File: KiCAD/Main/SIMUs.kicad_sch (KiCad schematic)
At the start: 10 parts, among them U14 BMI270, U15 BMI270, U16 BMI270

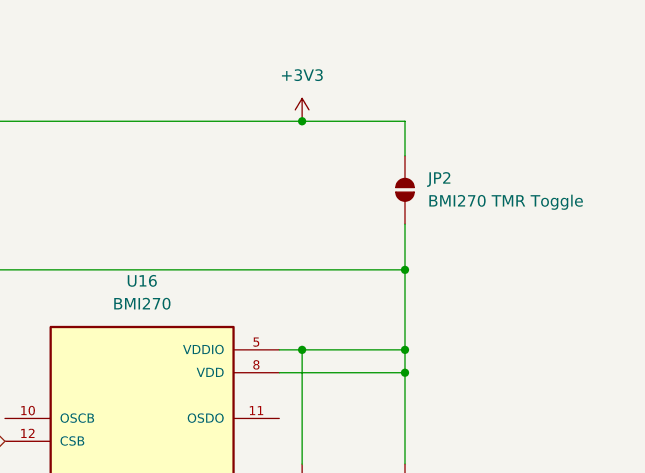
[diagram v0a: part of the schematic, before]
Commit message: Moved custom footprints into local KiCAD footprint library
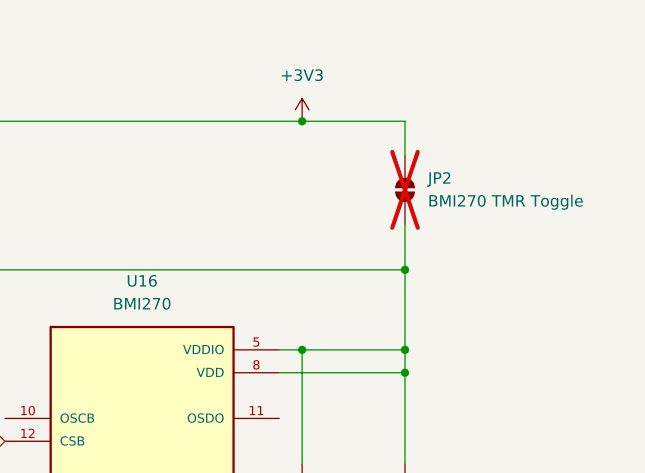
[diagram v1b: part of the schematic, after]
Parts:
- JP2: footprint Resistor_SMD:R_0603_1608Metric_Pad0.98x0.95mm_HandSolder -> Jumper:SolderJumper-2_P1.3mm_Open_TrianglePad1.0x1.5mm; now not fitted
- U14, U15, U16: footprint BMI270:XDCR_BMI270 -> LRI:XDCR_BMI270
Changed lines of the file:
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@@
 			)
 		)
-		(property "Footprint" "BMI270:XDCR_BMI270"
+		(property "Footprint" "LRI:XDCR_BMI270"
 			(at 157.48 106.68 0)
 			(effects
@@
 			)
 		)
-		(property "Footprint" "BMI270:XDCR_BMI270"
+		(property "Footprint" "LRI:XDCR_BMI270"
 			(at 219.71 74.93 0)
 			(effects
@@
 			)
 		)
-		(property "Footprint" "BMI270:XDCR_BMI270"
+		(property "Footprint" "LRI:XDCR_BMI270"
 			(at 157.48 46.99 0)
 			(effects
@@
 		(in_bom no)
 		(on_board yes)
-		(dnp no)
+		(dnp yes)
 		(fields_autoplaced yes)
 		(property "Reference" "JP2"
@@
 			)
 		)
-		(property "Footprint" "Resistor_SMD:R_0603_1608Metric_Pad0.98x0.95mm_HandSolder"
+		(property "Footprint" "Jumper:SolderJumper-2_P1.3mm_Open_TrianglePad1.0x1.5mm"
 			(at 248.92 39.37 0)
 			(effects

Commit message: Layout and routing
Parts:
- JP2: footprint Jumper:SolderJumper-2_P1.3mm_Open_TrianglePad1.0x1.5mm -> Jumper:SolderJumper-2_P1.3mm_Open_RoundedPad1.0x1.5mm
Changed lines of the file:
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@@
 			)
 		)
-		(property "Footprint" "Jumper:SolderJumper-2_P1.3mm_Open_TrianglePad1.0x1.5mm"
+		(property "Footprint" "Jumper:SolderJumper-2_P1.3mm_Open_RoundedPad1.0x1.5mm"
 			(at 248.92 39.37 0)
 			(effects

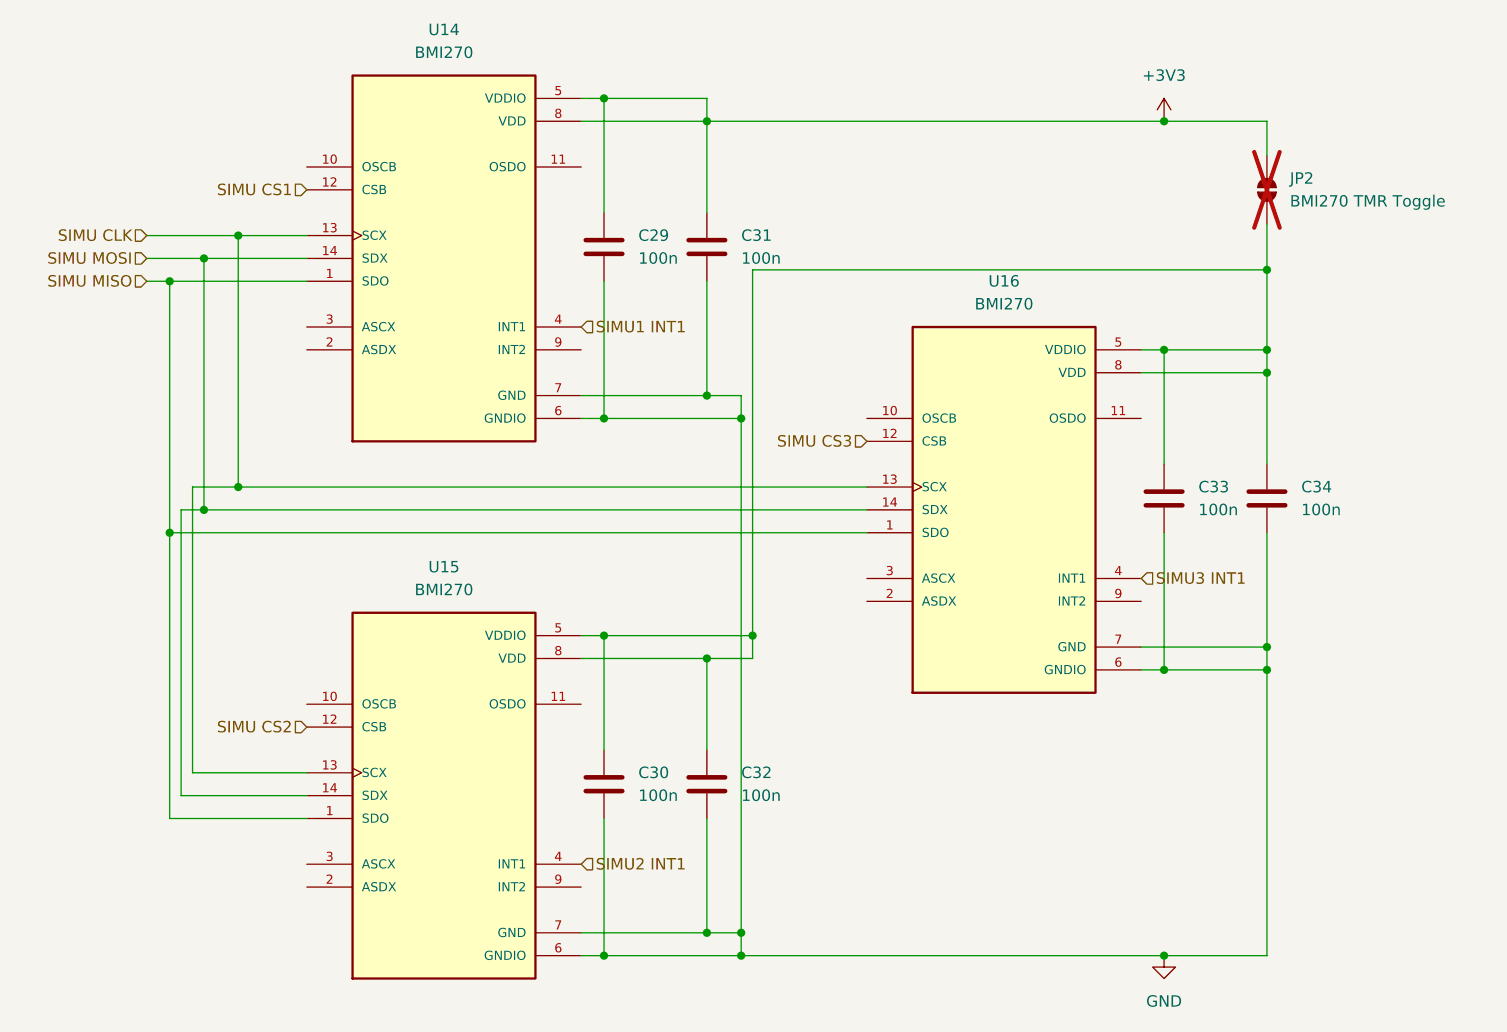
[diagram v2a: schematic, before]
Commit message: Reorganize libraries into LRI.pretty, replace BMI270 with BMI323
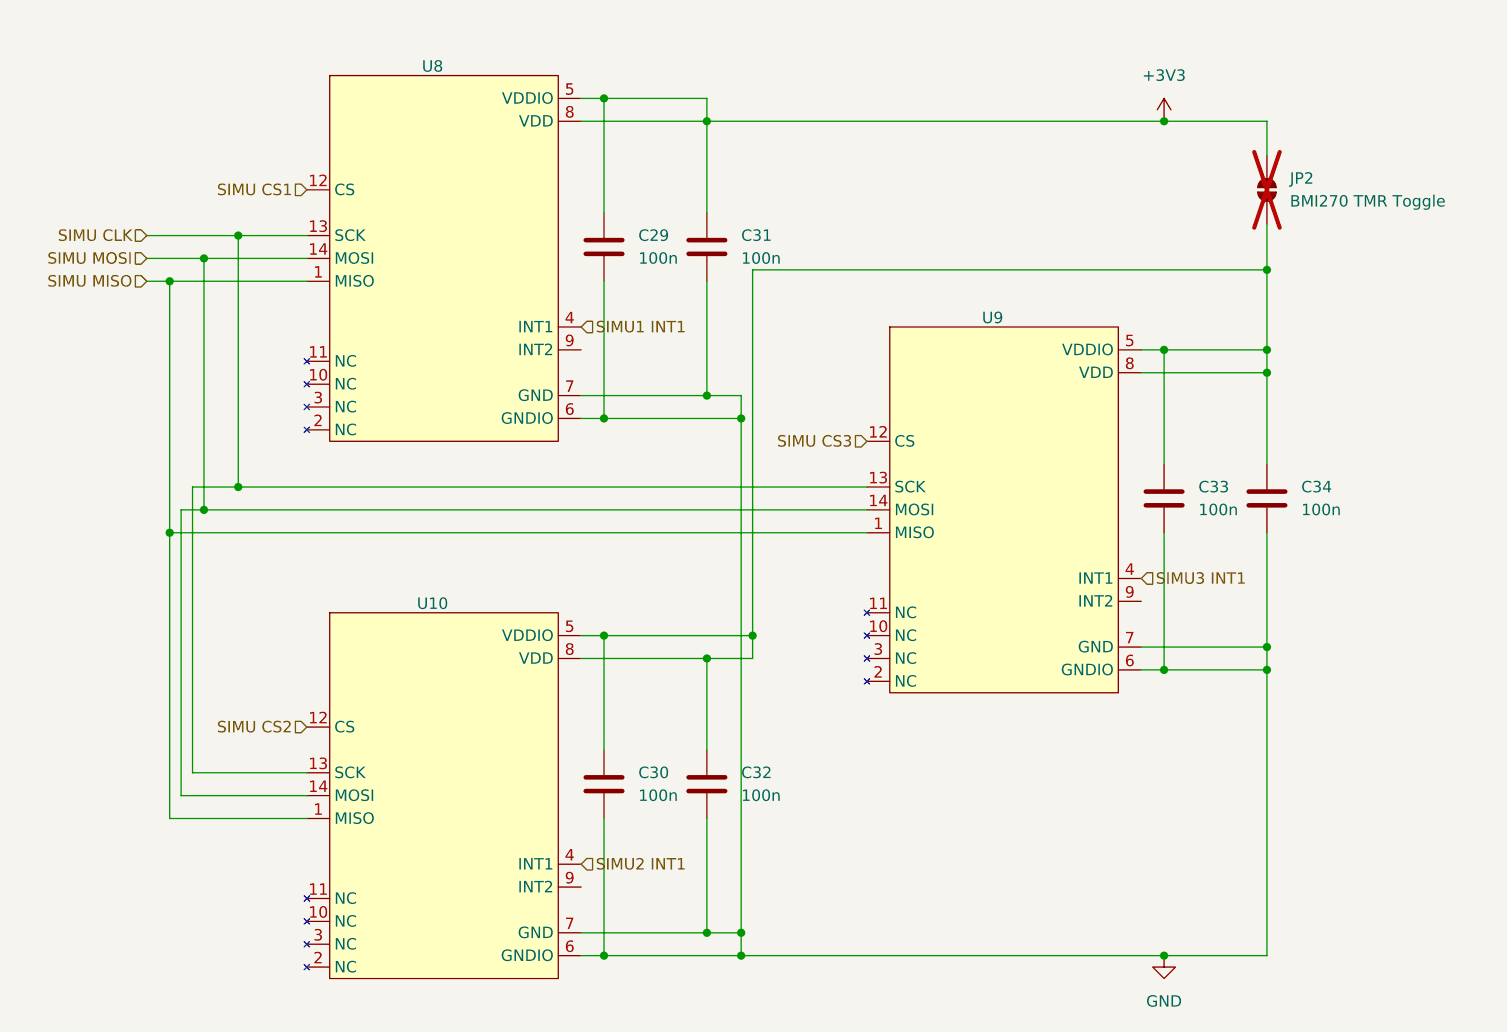
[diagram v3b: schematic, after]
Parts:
- removed U14, U15, U16: BMI270, LRI:XDCR_BMI270, symbol BMI270:BMI270
- added U10, U8, U9: ~, LRI:BMI323, symbol BMI323:BMI323
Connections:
- net +3V3: now also U8.5 (VDDIO), U8.8 (VDD)
- net GND: now also U10.6 (GNDIO), U10.7 (GND), U8.6 (GNDIO), U8.7 (GND), U9.6 (GNDIO), U9.7 (GND)
- net SIMU CLK: now also U10.13 (SCK), U8.13 (SCK), U9.13 (SCK)
- net SIMU CS1: now also U8.12 (CS)
- net SIMU CS2: now also U10.12 (CS)
- net SIMU CS3: now also U9.12 (CS)
- net SIMU MISO: now also U10.1 (MISO), U8.1 (MISO), U9.1 (MISO)
- net SIMU MOSI: now also U10.14 (MOSI), U8.14 (MOSI), U9.14 (MOSI)
- net SIMU1 INT1: now also U8.4 (INT1)
- net SIMU2 INT1: now also U10.4 (INT1)
- net SIMU3 INT1: now also U9.4 (INT1)
- net at C30.1, C32.1, C33.1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: now also U10.5 (VDDIO), U10.8 (VDD), U9.5 (VDDIO), U9.8 (VDD)
